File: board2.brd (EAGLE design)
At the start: 100 x 80 mm, 74 parts, among them Q1 7.68M, Q2 16MHz

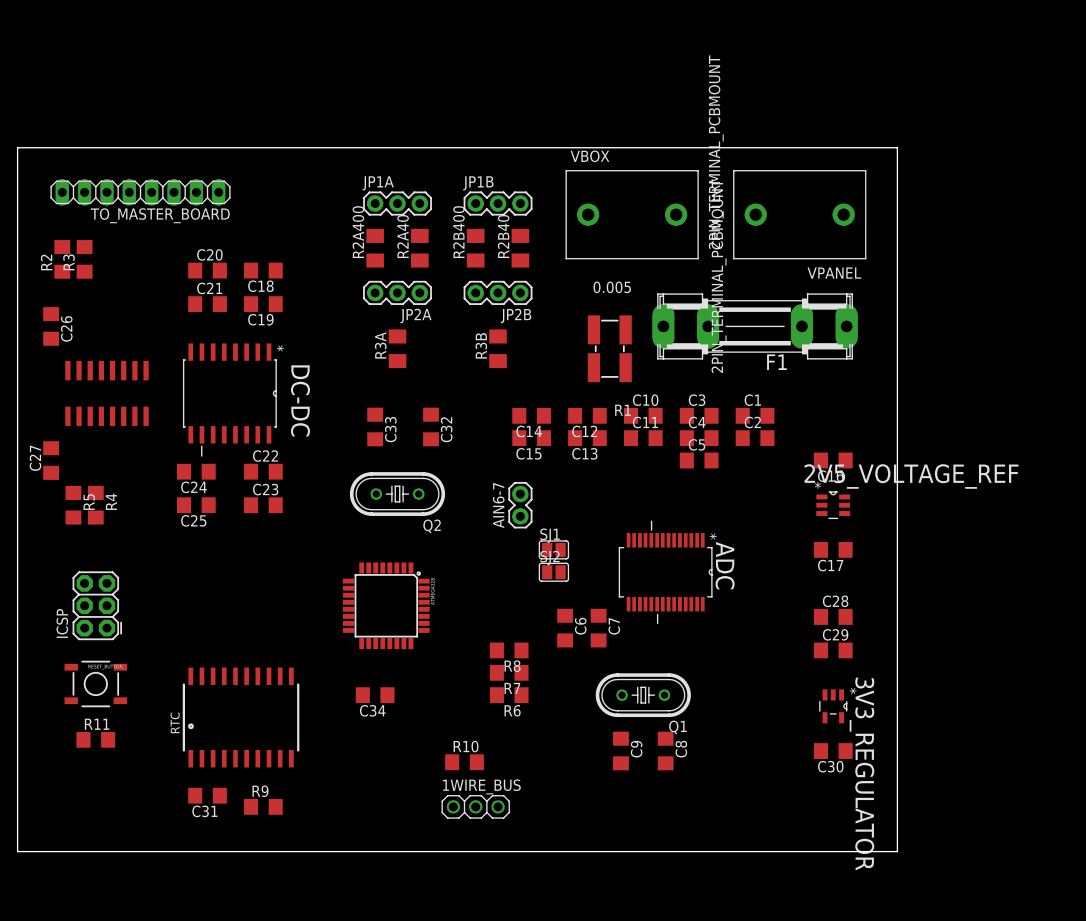
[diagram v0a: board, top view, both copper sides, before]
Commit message: Added GND planes and continue working on tracing..
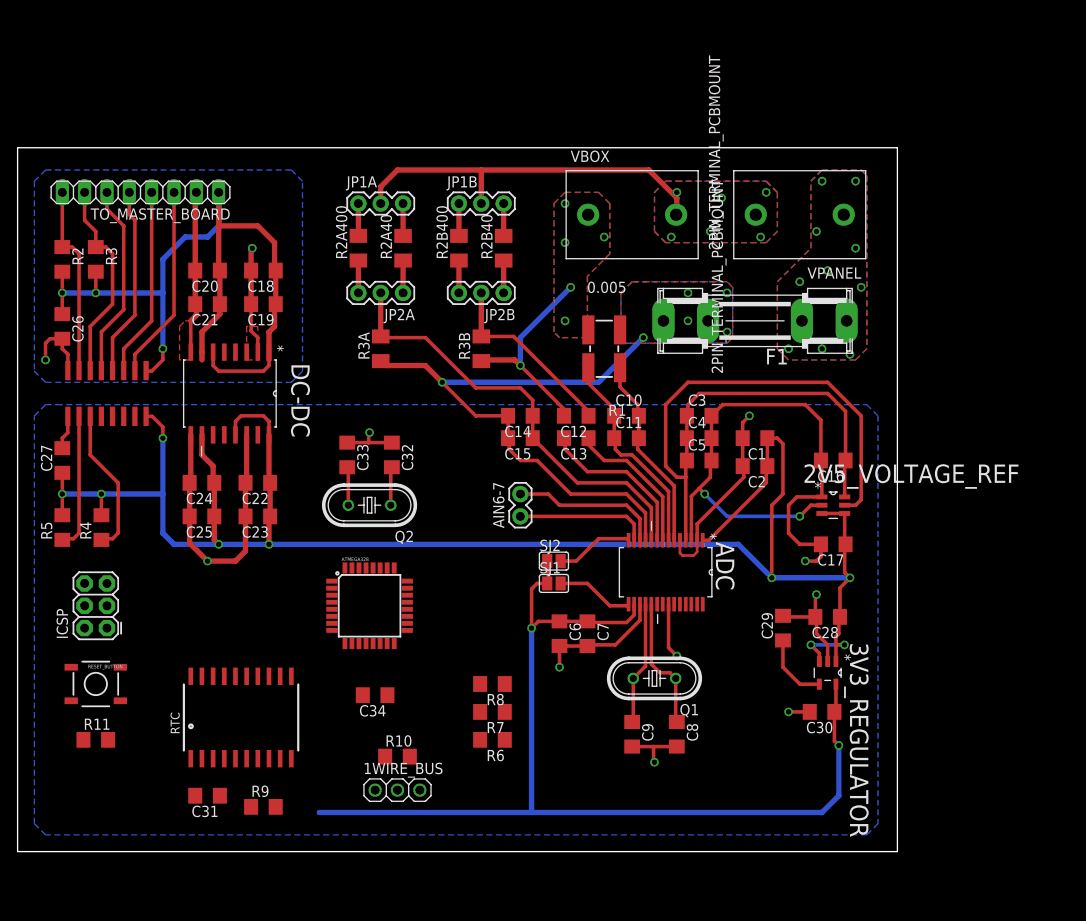
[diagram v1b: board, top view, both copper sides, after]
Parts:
- moved 1WIRE_BUS 9.09 mm to (43.2, 6.99)
- moved R10 7.65 mm to (43.2, 10.8)
- moved C29 6.25 mm to (87.0, 25.4), turned to 90 degrees
- moved C32 5.46 mm to (42.5, 45.1)
- moved R6 5.43 mm to (54.0, 12.7)
- moved R7 4.84 mm to (54.0, 15.9)
- moved C30 4.62 mm to (91.4, 15.9)
- moved C33 4.49 mm to (37.5, 45.1)
- moved R8 4.26 mm to (54.0, 19.1)
- moved 3V3_REGULATOR 3.86 mm to (92.1, 20.3)
- moved SJ1 3.81 mm to (61.0, 30.5)
- moved Q2 3.42 mm to (40.0, 39.4)
- moved C2 3.18 mm to (83.8, 43.8), turned to 180 degrees
- moved R5 2.84 mm to (5.08, 36.8), turned to 90 degrees
- moved R4 2.62 mm to (9.53, 36.8), turned to 90 degrees
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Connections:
- new net GND_SENSE: 2V5_VOLTAGE_REF.2
- new net V_SENSE: 2V5_VOLTAGE_REF.5
- net GND_ISO: no longer 2V5_VOLTAGE_REF.2
- net VREF_2V5: no longer 2V5_VOLTAGE_REF.5
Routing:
- net 5V_ISO: track 0.00 -> 207.4 mm, vias 0 -> 9
- net GND_ISO: track 0.00 -> 153.6 mm, vias 0 -> 8
- net 3V3: track 0.00 -> 116.8 mm, vias 0 -> 2
- net 5V: track 0.00 -> 95.2 mm, vias 0 -> 3
- net VREF_2V5: track 0.00 -> 90.7 mm
- net AIN5: track 0.00 -> 67.5 mm, vias 0 -> 6
- net AIN4: track 0.00 -> 50.0 mm
- net AIN3: track 0.00 -> 43.9 mm, vias 0 -> 6
- net VBUS1: track 0.00 -> 43.4 mm, vias 0 -> 6
- net GND: track 0.00 -> 38.6 mm, vias 0 -> 2
- net AIN2: track 0.00 -> 37.9 mm
- net AIN1: track 0.00 -> 24.2 mm
- net SDA: track 0.00 -> 23.3 mm
- net AIN0: track 0.00 -> 22.3 mm
- net OUT2: track 0.00 -> 22.1 mm
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- added copper zone on layer 1, net AIN3
- added copper zone on layer 16, net AIN3
- added copper zone on layer 1, net AIN5
- added copper zone on layer 16, net AIN5
- added copper zone on layer 1, net GND
- added copper zone on layer 16, net GND
- added copper zone on layer 16, net GND_ISO
- added copper zone on layer 1, net VBUS1
- added copper zone on layer 16, net VBUS1
- added copper zone on layer 1, net VBUS2
- added copper zone on layer 16, net VBUS2

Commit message: I think I finished routing
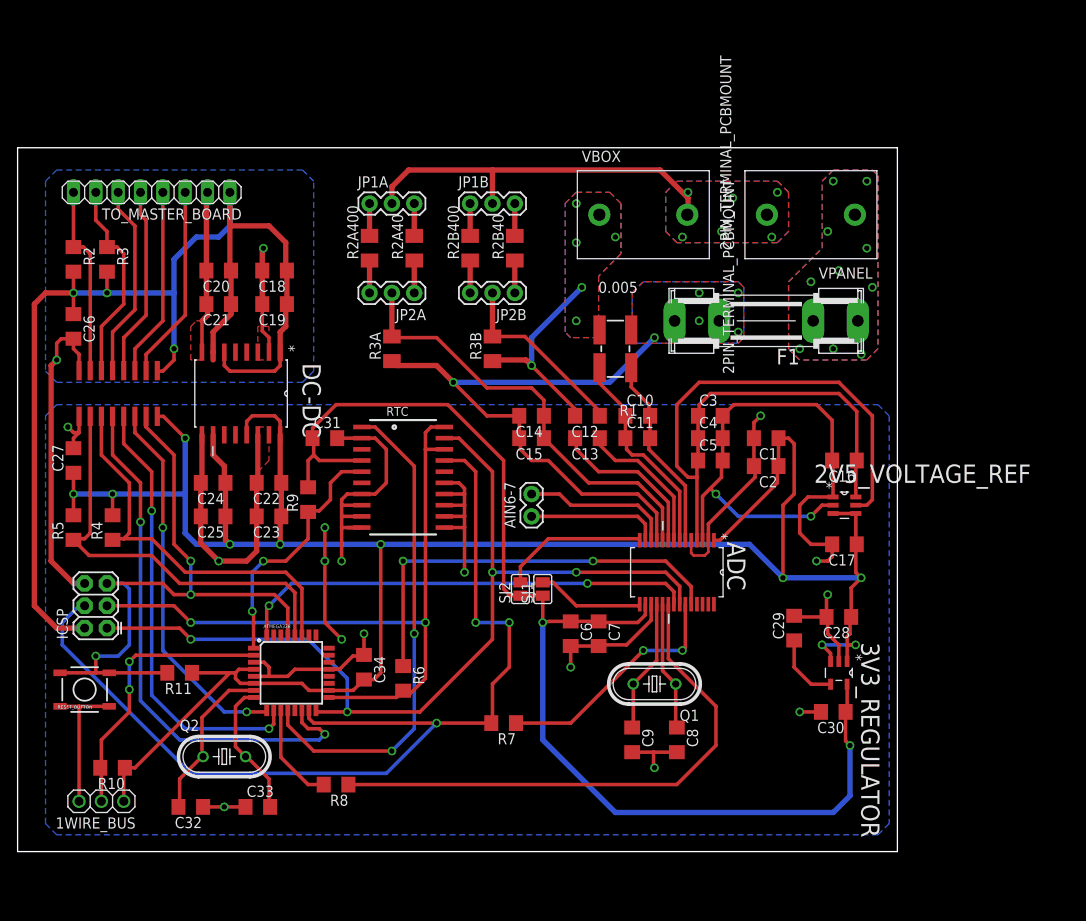
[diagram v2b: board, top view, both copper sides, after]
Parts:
- moved C32 46.1 mm to (19.7, 5.08), turned to 180 degrees
- moved C31 42.8 mm to (34.9, 47.0), turned to 0 degrees
- moved C33 41.3 mm to (27.3, 5.08), turned to 0 degrees
- moved R9 35.3 mm to (33.0, 40.0), turned to 90 degrees
- moved 1WIRE_BUS 33.7 mm to (9.53, 5.71), turned to 180 degrees
- moved Q2 33.0 mm to (23.5, 10.8), turned to 0 degrees
- moved RTC 32.9 mm to (43.8, 42.5), turned to 270 degrees
- moved R10 32.4 mm to (10.8, 9.53), turned to 180 degrees
- moved R8 21.1 mm to (36.2, 7.62)
- moved R6 12.3 mm to (43.8, 19.7), turned to 270 degrees
- moved R11 12.2 mm to (18.4, 20.3), turned to 180 degrees
- moved ATMEGA328 11.7 mm to (31.1, 20.3)
- moved SJ2 4.96 mm to (57.1, 29.8), turned to 90 degrees
- moved C34 3.42 mm to (39.4, 21.0), turned to 270 degrees
- moved R7 1.80 mm to (55.2, 14.6)
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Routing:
- net MOSI: track 0.00 -> 116.0 mm, vias 0 -> 3
- net GND_ISO: track 153.6 -> 255.4 mm, vias 8 -> 15
- net MISO: track 6.28 -> 107.1 mm, vias 1 -> 4
- net SCLK: track 0.00 -> 81.7 mm, vias 0 -> 2
- net RESET: track 0.00 -> 74.7 mm, vias 0 -> 3
- net 5V_ISO: track 207.4 -> 269.3 mm, vias 9 -> 10
- net N$16: track 0.00 -> 61.9 mm
- net OUT2_ISO: track 0.00 -> 61.2 mm, vias 0 -> 2
- net RTC_CS: track 0.00 -> 55.9 mm, vias 0 -> 2
- net ADC_DRDY: track 0.00 -> 52.3 mm, vias 0 -> 2
- net OUT1_ISO: track 0.00 -> 50.2 mm, vias 0 -> 2
- net N$1: track 0.00 -> 47.9 mm, vias 0 -> 2
- net 5V: track 95.2 -> 141.2 mm
- net IN2_ISO: track 0.00 -> 42.7 mm, vias 0 -> 2
- net SCL_ISO: track 15.5 -> 48.0 mm
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- added copper zone on layer 1, net GND_ISO

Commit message: Small details changed
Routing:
- net AIN5: vias 6 -> 7
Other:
- board text added: "PV Measurements PCB v2.0"
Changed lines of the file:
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@@
 <wire x1="100" y1="80" x2="0" y2="80" width="0" layer="20"/>
 <wire x1="0" y1="80" x2="0" y2="0" width="0" layer="20"/>
+<text x="38.735" y="1.905" size="1.778" layer="112">PV Measurements PCB v2.0</text>
 </plain>
 <attributes>
@@
 <via x="77.47" y="60.325" extent="1-16" drill="0.6"/>
 <wire x1="67.31" y1="53.34" x2="72.39" y2="58.42" width="0.6096" layer="16"/>
+<via x="71.755" y="62.865" extent="1-16" drill="0.6"/>
 </signal>
 <signal name="VBUS2">
@@
 <wire x1="20.955" y1="60.325" x2="20.955" y2="56.769" width="0.4064" layer="1"/>
 <polygon width="0.4064" layer="16" isolate="0.4064">
-<vertex x="4.445" y="53.34"/>
+<vertex x="2.54" y="53.34"/>
 <vertex x="32.385" y="53.34"/>
 <vertex x="33.655" y="54.61"/>
 <vertex x="33.655" y="76.2"/>
 <vertex x="32.385" y="77.47"/>
-<vertex x="4.445" y="77.47"/>
-<vertex x="3.175" y="76.2"/>
-<vertex x="3.175" y="54.61"/>
+<vertex x="2.54" y="77.47"/>
+<vertex x="1.27" y="76.2"/>
+<vertex x="1.27" y="54.61"/>
 </polygon>
 <wire x1="6.985" y1="54.67" x2="6.985" y2="56.515" width="0.4064" layer="1"/>
@@
 <contactref element="1WIRE_BUS" pad="3"/>
 <polygon width="0.6096" layer="16" isolate="0.4064">
-<vertex x="4.445" y="50.8"/>
+<vertex x="2.54" y="50.8"/>
 <vertex x="97.79" y="50.8"/>
 <vertex x="99.06" y="49.53"/>
 <vertex x="99.06" y="3.175"/>
 <vertex x="97.79" y="1.905"/>
-<vertex x="4.445" y="1.905"/>
-<vertex x="3.175" y="3.175"/>
-<vertex x="3.175" y="49.53"/>
+<vertex x="2.54" y="1.905"/>
+<vertex x="1.27" y="3.175"/>
+<vertex x="1.27" y="49.53"/>
 </polygon>
 <wire x1="27.305" y1="47.371" x2="27.305" y2="42.04" width="0.6096" layer="1"/>

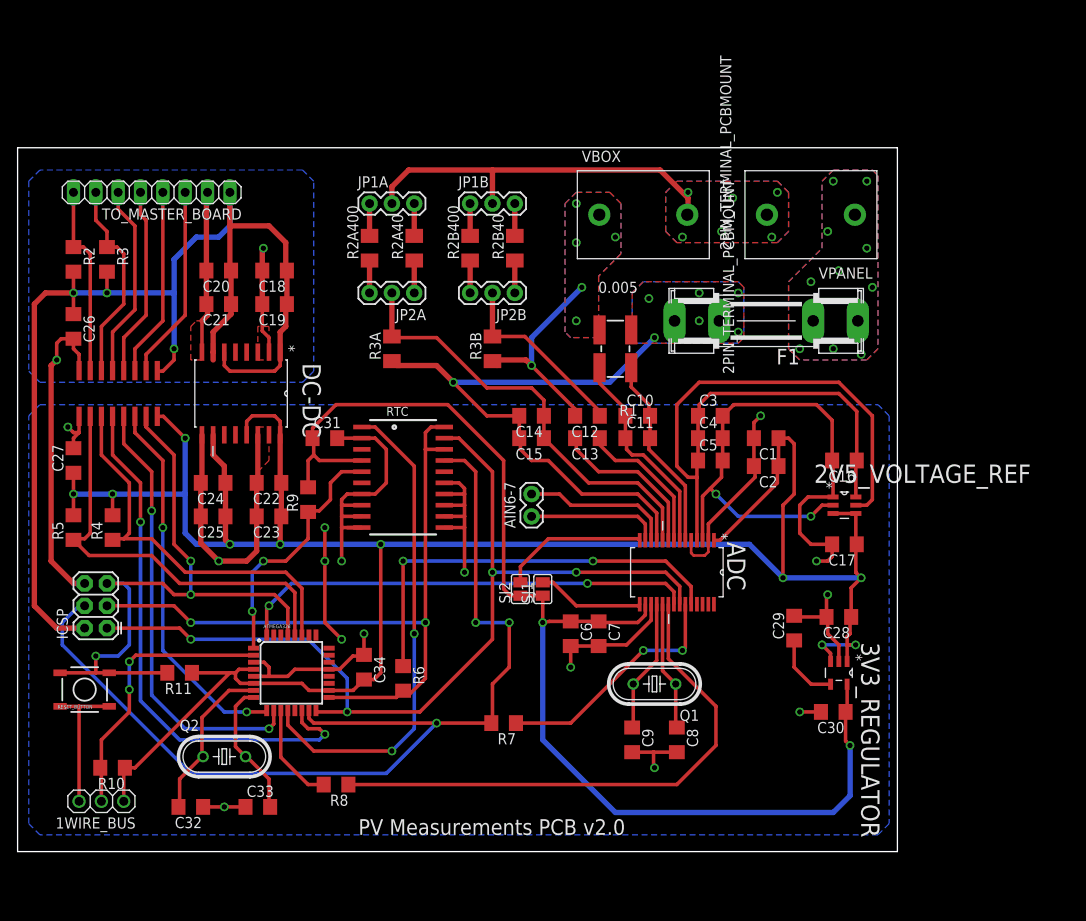
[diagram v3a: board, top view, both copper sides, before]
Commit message: added battery for RTC and small changes
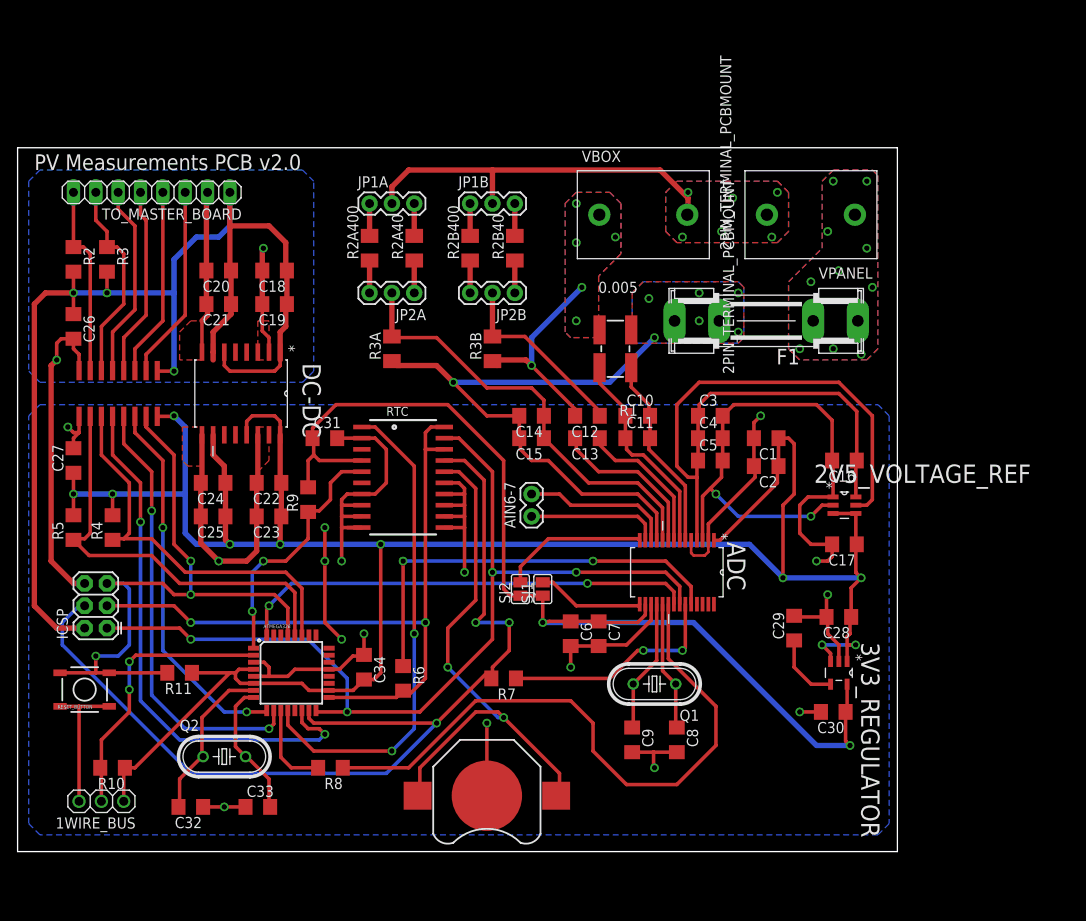
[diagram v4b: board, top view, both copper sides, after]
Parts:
- added BAT1: 3V, SparkFun-Electromechanical:BATTCON_12MM
- moved R7 5.08 mm to (55.2, 19.7)
- moved R8 2.01 mm to (35.6, 9.53)
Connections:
- new net N$22: BAT1.PWR@1, RTC.16
- net GND_ISO: now also BAT1.GND
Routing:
- net N$22: track 0.00 -> 62.0 mm, vias 0 -> 2
- net 3V3: track 139.6 -> 122.1 mm
- net N$16: track 61.9 -> 71.5 mm
- net GND_ISO: track 255.4 -> 263.7 mm, vias 15 -> 16
- net N$14: track 27.7 -> 25.6 mm
- net MOSI: track 116.0 -> 114.4 mm
- net ADC_CS: track 11.5 -> 10.0 mm
- net 5V_ISO: track 269.3 -> 270.1 mm
- net 5V: track 141.2 -> 142.0 mm
